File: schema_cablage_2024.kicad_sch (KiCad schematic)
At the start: 64 parts, among them M1 am-3775a, M2 Motor_DC, P1 SB-50, P2 SB-50, SW1 SW_SPDT, SW2 SW_SPDT, U1 VEX_CTRE_Talon_SRX, U11 REV_Spark_MAX, U12 Limelight, U13 REV_Spark_MAX, U14 Kauai_navX2-MXP, U2 Magnetic_Encoder_AM-3749, U4 CTRE_Pneumatics_Control_Module, U6 Banner_Photoelectric_Sensor_Q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, U9 RoboRIO

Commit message: MaJ librairie + schema
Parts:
- gave numbers to parts that had none: 34
- renumbered F7 to F12, F8 to F13, F9 to F14, F3 to F4, F4 to F5, M2 to M6, M1 to M7, U9 to U11, U12 to U13, U14 to U16, U11 to U17, U13 to U18, U1 to U6, U4 to U7, U2 to U8, U6 to U9
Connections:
- net at U8. (PWM): now also U6. (VIN)
- net at U14. (PWM): no longer U12. (VIN)
- new net: U6. (VIN), U8. (PWM) (x2)
- new net: M11. (IN_C), U17. (VIN-)
- new net: U12. (VIN), U14. (PWM) (x3)
- new net: M12. (IN_C), U18. (VIN-)
- new net: M2. (IN_C), U2. (VIN-)
- new net: M1. (IN_C), U1. (VIN-)
- now unconnected: U14. (PWM), U14. (PWM)
- no-connect marks 42 -> 44
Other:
- moved on the sheet: GN1, GN2, GN3

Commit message: Finalisation du symbole PDH, debut du schema 2024
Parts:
- removed F1: 20A, symbol Device:Fuse_Small
- removed F10, F4, F5, F6, F7, F8, F9: 30A, symbol Device:Polyfuse_Small
- removed F12, F13, F2, F3: 40A, symbol Device:Polyfuse
- removed L1, L2, L3: Solenoid, symbol Device:ElectromagneticActor
- removed M10, M3, M4, M5, M7, M8: am-3775a, symbol Motor:Motor_DC
- removed M11, M12: REV_NEO_Brushless_Motor, symbol FRC_Components:REV_NEO_Brushless_Motor
- removed M6: Motor_DC, symbol Motor:Motor_DC
- removed PS1: CTRE_Power_Distribution_Panel, symbol FRC_Components:CTRE_Power_Distribution_Panel
- removed S1: SW_Pressure_NC, symbol FRC_Components:SW_Pressure_NC
- removed SW1, SW2: SW_SPDT, symbol Switch:SW_SPDT
- removed U10, U15, U3, U4, U5: VEX_CTRE_Victor_SPX, symbol FRC_Components:VEX_CTRE_Victor_SPX
- removed U17, U18: REV_Spark_MAX, symbol FRC_Components:REV_Spark_MAX
- removed U6: VEX_CTRE_Talon_SRX, symbol FRC_Components:VEX_CTRE_Talon_SRX
- removed U7: CTRE_Pneumatics_Control_Module, symbol FRC_Components:CTRE_Pneumatics_Control_Module
- removed U8: Magnetic_Encoder_AM-3749, symbol FRC_Components:Magnetic_Encoder_AM-3749
- added D? (x6): NeoPixel_THT, symbol LED:NeoPixel_THT
- added F? (x4): 40A, symbol Device:Polyfuse_Small
- added F? (x3): 30A, symbol Device:Polyfuse_Small
- added M? (x6): REV_NEO_Brushless_Motor, symbol FRC_Components:REV_NEO_Brushless_Motor
- added PS?: REV_Power_Distribution_Hub, symbol FRC_Components:REV_Power_Distribution_Hub
- added U? (x6): REV_Spark_MAX, symbol FRC_Components:REV_Spark_MAX
- F11: value 5A -> 30A
- U13: value Limelight -> Limelight 3
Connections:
- net CANH: now also PS?. (VOUT9), U?. (VIN-), U?. (VIN-), U?. (VIN-), U?. (VIN-), U?. (VIN-), U?. (VIN-); no longer U11. (~{SPI_CS3})
- net CANL: now also PS?. (VOUT9), U?. (VIN-), U?. (VIN-), U?. (VIN-), U?. (VIN-), U?. (VIN-), U?. (VIN-); no longer U11. (~{SPI_CS3})
- net SIG: now also D?.1 (DOUT), D?.1 (DOUT), D?.1 (DOUT), D?.1 (DOUT), D?.4 (DIN), D?.4 (DIN), D?.4 (DIN), D?.4 (DIN), D?.4 (DIN), D?.4 (DIN)
- net V+: now also D?.3 (VDD), D?.3 (VDD), D?.3 (VDD), D?.3 (VDD), D?.3 (VDD), D?.3 (VDD), PS?. (VOUT9), U?. (VIN-), U?. (VIN-), U?. (VIN-), U?. (VIN-), U?. (VIN-), U?. (VIN-); no longer U12. (VIN), U13. (V-)
- net V-: now also D?.2 (GND), D?.2 (GND), D?.2 (GND), D?.2 (GND), D?.2 (GND), D?.2 (GND), PS?. (VOUT9), U?. (VIN-), U?. (VIN-), U?. (VIN-), U?. (VIN-), U?. (VIN-), U?. (VIN-); no longer U13. (V-)
- net ΦA: now also M?. (IN_C), M?. (IN_C), M?. (IN_C), M?. (IN_C), M?. (IN_C), M?. (IN_C), U?. (VIN-), U?. (VIN-), U?. (VIN-), U?. (VIN-), U?. (VIN-), U?. (VIN-)
- net ΦB: now also M?. (IN_C), M?. (IN_C), M?. (IN_C), M?. (IN_C), M?. (IN_C), M?. (IN_C), U?. (VIN-), U?. (VIN-), U?. (VIN-), U?. (VIN-), U?. (VIN-), U?. (VIN-)
- net ΦC: now also M?. (IN_C), M?. (IN_C), M?. (IN_C), M?. (IN_C), M?. (IN_C), M?. (IN_C), U?. (VIN-), U?. (VIN-), U?. (VIN-), U?. (VIN-), U?. (VIN-), U?. (VIN-)
- net at SW4.2 (B): no longer U12. (VIN)
- net at U14. (PWM): now also SW5.1 (A), SW6.1 (A); no longer U12. (VIN)
- net at SW3.2 (B): no longer U12. (VIN)
- net at F11.1: now also PS?. (VOUT9)
- net at F11.2: now also PS?. (VOUT9)
- removed net USB: U11. (~{SPI_CS3}), U16. (μUSB)
- new net: M?. (IN_C), U?. (VIN-) (x6)
- new net: F?.1, PS?. (VOUT9) (x7)
- new net: F?.2, PS?. (VOUT9) (x7)
- new net: M2. (IN_C), U2. (VIN-)
- new net: M1. (IN_C), U1. (VIN-)
- no-connect marks 44 -> 104
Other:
- note added: "Et ainsi de suite pour le reste des bandes de DEL"
- note added: "SPARK MAX SWERVE DIRECTION ARRIERE DROIT"
- note added: "SPARK MAX SWERVE DIRECTION ARRIERE GAUCHE"
- note added: "SPARK MAX SWERVE DIRECTION AVANT DROIT"
- note added: "SPARK MAX SWERVE DIRECTION AVANT GAUCHE"
- note added: "SPARK MAX SWERVE PROPULSION ARRIERE DROIT"
- note added: "SPARK MAX SWERVE PROPULSION ARRIERE GAUCHE"
- note added: "SPARK MAX SWERVE PROPULSION AVANT DROIT"
- note added: "SPARK MAX SWERVE PROPULSION AVANT GAUCHE"
- note removed: "Compresseur"
- note removed: "FWD LIMIT"
- note removed: "Interrupteur à pression — réservoir d'air"
- note removed: "PCM (CAN 0)"
- note removed: "PDP (CAN 0)"
- note removed: "REV LIMIT"
- note removed: "SPARK MAX BASE (DROIT 1)"
- note removed: "TALON SRX ROTATION RAMASSEUR (CAN 6)"
- note removed: "VICTOR SPX RAMASSEUR (DROIT, CAN 7)"
- note removed: "VICTOR SPX RAMASSEUR (GAUCHE, CAN 3)"
- note removed: "VICTOR SPX ÉLÉVATEUR (#2, ESCLAVE, CAN 5)"
- note removed: "VICTOR SPX ÉLÉVATEUR (#3, ESCLAVE, CAN 14)"
- note removed: "VICTOR SPX ÉLÉVATEUR (#4, ESCLAVE, CAN 15)"
- note removed: "VÉRINS BASCULEUR"
- note removed: "VÉRINS RAMASSEUR"
- note removed: "VÉRINS ÉLÉVATEUR"
- moved on the sheet: B1, CB1, DS1, F11, F14, GN1, GN2, GN3, M1, M2, M9, P1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

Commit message: v1.0
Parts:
- removed D? (x6): NeoPixel_THT, symbol LED:NeoPixel_THT
- removed F14: 10A, symbol Device:Fuse_Small
- removed SW3, SW4, SW5, SW6: SW_SPDT, symbol Switch:SW_SPDT
- removed U14: Magnetic_Encoder_AM-3749, symbol FRC_Components:Magnetic_Encoder_AM-3749
- added D? (x4): NeoPixel_THT, symbol LED:NeoPixel_THT
- added F10, F12, F13, F14, F5, F6, F7, F8, F9: 30A, symbol Device:Polyfuse_Small
- added F2: 10A, symbol Device:Polyfuse_Small
- added F3, F4: 5A, symbol Device:Fuse_Small
- added F?: 10A, symbol Device:Fuse_Small
- added M10, M11, M5, M6, M7, M8: REV_NEO_Brushless_Motor, symbol FRC_Components:REV_NEO_Brushless_Motor
- added M3, M4: am-3775a, symbol Motor:Motor_DC
- added U10, U14, U15, U17, U18, U19: REV_Spark_MAX, symbol FRC_Components:REV_Spark_MAX
- added U3: Limelight 2+, symbol FRC_Components:Limelight
- added U4, U6, U8: CTRE_SRX_Mag_Encoder, symbol FRC_Components:CTRE_SRX_Mag_Encoder
- added U5, U7: VEX_CTRE_Talon_SRX, symbol FRC_Components:VEX_CTRE_Talon_SRX
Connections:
- net CANH: now also U10. (VIN-), U14. (VIN-), U15. (VIN-), U17. (VIN-), U18. (VIN-), U19. (VIN-), U5. (VIN), U7. (VIN)
- net CANL: now also U10. (VIN-), U14. (VIN-), U15. (VIN-), U17. (VIN-), U18. (VIN-), U19. (VIN-), U5. (VIN), U7. (VIN)
- net ETH: now also U3. (V-)
- net SIG: now also D?.1 (DOUT), D?.1 (DOUT), D?.4 (DIN), D?.4 (DIN), D?.4 (DIN), D?.4 (DIN)
- net V+: now also U12. (VIN), U13. (V-), D?.3 (VDD), D?.3 (VDD), D?.3 (VDD), D?.3 (VDD), U10. (VIN-), U14. (VIN-), U15. (VIN-), U17. (VIN-), U18. (VIN-), U19. (VIN-), U3. (V-), U5. (VIN), U7. (VIN); no longer M9.1 (+)
- net V-: now also U13. (V-), D?.2 (GND), D?.2 (GND), D?.2 (GND), D?.2 (GND), U10. (VIN-), U14. (VIN-), U15. (VIN-), U17. (VIN-), U18. (VIN-), U19. (VIN-), U3. (V-), U5. (VIN), U7. (VIN); no longer M9.2 (-)
- net ΦA: now also M10. (IN_C), M11. (IN_C), M5. (IN_C), M6. (IN_C), M7. (IN_C), M8. (IN_C), U10. (VIN-), U14. (VIN-), U15. (VIN-), U17. (VIN-), U18. (VIN-), U19. (VIN-)
- net ΦB: now also M10. (IN_C), M11. (IN_C), M5. (IN_C), M6. (IN_C), M7. (IN_C), M8. (IN_C), U10. (VIN-), U14. (VIN-), U15. (VIN-), U17. (VIN-), U18. (VIN-), U19. (VIN-)
- net ΦC: now also M10. (IN_C), M11. (IN_C), M5. (IN_C), M6. (IN_C), M7. (IN_C), M8. (IN_C), U10. (VIN-), U14. (VIN-), U15. (VIN-), U17. (VIN-), U18. (VIN-), U19. (VIN-)
- new net: F4.1, PS?. (VOUT9)
- new net: F4.2, PS?. (VOUT9)
- new net: M11. (IN_C), U19. (VIN-)
- new net: F9.1, PS?. (VOUT9)
- new net: F9.2, PS?. (VOUT9)
- new net: M?. (IN_C), U?. (VIN-) (x6)
- new net: M6. (IN_C), U14. (VIN-)
- new net: M10. (IN_C), U18. (VIN-)
- new net: F14.1, PS?. (VOUT9)
- new net: F14.2, PS?. (VOUT9)
- new net: F10.1, PS?. (VOUT9)
- new net: F10.2, PS?. (VOUT9)
- new net: M7. (IN_C), U15. (VIN-)
- new net: F8.1, PS?. (VOUT9)
- new net: F8.2, PS?. (VOUT9)
- new net: F13.1, PS?. (VOUT9)
- new net: F13.2, PS?. (VOUT9)
- new net: M5. (IN_C), U10. (VIN-)
- new net: F5.1, PS?. (VOUT9)
- new net: F5.2, PS?. (VOUT9)
- new net: M2. (IN_C), U2. (VIN-)
- new net: M1. (IN_C), U1. (VIN-)
- new net: F?.1, PS?. (VOUT9)
- new net: F?.2, PS?. (VOUT9)
- new net: F6.1, PS?. (VOUT9)
- new net: F6.2, PS?. (VOUT9)
- new net: F12.1, PS?. (VOUT9)
- new net: F12.2, PS?. (VOUT9)
- new net: F3.1, PS?. (VOUT9)
- new net: F3.2, PS?. (VOUT9)
- new net: F2.1, PS?. (VOUT9)
- new net: F2.2, PS?. (VOUT9)
- new net: F7.1, PS?. (VOUT9)
- new net: F7.2, PS?. (VOUT9)
- new net: M8. (IN_C), U17. (VIN-)
- new net M+: M3.1 (+), M4.1 (+), M9.1 (+), U12. (VIN), U5. (VIN), U7. (VIN)
- new net M-: M3.2 (-), M4.2 (-), M9.2 (-), U12. (VIN), U5. (VIN), U7. (VIN)
- no-connect marks 104 -> 170
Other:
- note added: "24 DEL/bande. Seulement 2 de représentées."
- note added: "ARRIERE"
- note added: "ATTENTION: Certaines des broches (3, 6) des breakouts ne doivent pas être utilisées."
- note added: "AVANT"
- note added: "Breakout board"
- note added: "Câble gainé pour l'articulation 8 fils seulement au lieu de 10"
- note added: "Les broches de même numéro sont reliées."
- note added: "Nappe de fils plate"
- note added: "SPARK MAX ELEVATEUR DROIT"
- note added: "SPARK MAX ELEVATEUR GAUCHE"
- note added: "SPARK MAX PROPULSION LANCEUR DROIT"
- note added: "SPARK MAX PROPULSION LANCEUR GAUCHE"
- note added: "SPARK MAX RAMASSEUR COURROIE DU BAS"
- note added: "SPARK MAX RAMASSEUR COURROIE DU HAUT"
- note added: "TALON SRX ANGLE LANCEUR"
- note added: "TALON SRX BRAS PRIMAIRE"
- note added: "TALON SRX BRAS SECONDAIRE"
- note removed: "Et ainsi de suite pour le reste des bandes de DEL"
- note removed: "FWD LIMIT 1"
- note removed: "FWD LIMIT 2"
- note removed: "REV LIMIT 1"
- note removed: "REV LIMIT 2"
- note removed: "SPARK MAX BASE (DROIT 2)"
- note removed: "SPARK MAX BASE (GAUCHE 1)"
- note removed: "TALON SRX ÉLÉVATEUR (#1, MAÎTRE, CAN 4)"
- title: Schéma de câblage Swerve 2024 -> Schéma de câblage Disc-O 2024
- moved on the sheet: CB1, DS1, F11, F?, GN1, GN2, GN3, M1, M2, M9, M?, P1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

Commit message: v1.1
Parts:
- removed M1, M2, M? (x6): REV_NEO_Brushless_Motor, symbol FRC_Components:REV_NEO_Brushless_Motor
- removed U1, U2, U? (x6): REV_Spark_MAX, symbol FRC_Components:REV_Spark_MAX
- added U4: Banner_Photoelectric_Sensor_QS18VN6LP, symbol FRC_Components:Banner_Photoelectric_Sensor_QS18VN6LP
- F6: renamed from F2; value 10A -> 20A
- gave numbers to parts that had none: 13
- renumbered F4 to F11, F5 to F14, F6 to F15, F13 to F16, F12 to F17, F7 to F18, F8 to F19, F11 to F2, F14 to F3, F10 to F4, F9 to F5, F3 to F9, GN3 to GN1, GN1 to GN2, GN2 to GN3, M6 to M1, M5 to M2, M4 to M3, M9 to M4, M3 to M5, M7 to M6, M8 to M7, M10 to M8, M11 to M9, U14 to U1, U16 to U10, U8 to U11, U4 to U12, U5 to U13, U15 to U14, U17 to U15, U18 to U16, U19 to U17, U6 to U18, U10 to U2, U9 to U3, U11 to U5, U3 to U6, U13 to U7, U7 to U8, U12 to U9
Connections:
- net CANH: now also U5. (~{SPI_CS3})
- net CANL: now also U5. (~{SPI_CS3})
- net SIG: now also U4. (V-)
- net V+: now also U4. (V-)
- net V-: now also U4. (V-)
- new net: M9. (IN_C), U17. (VIN-)
- new net: M1. (IN_C), U1. (VIN-)
- new net: M8. (IN_C), U16. (VIN-)
- new net: M6. (IN_C), U14. (VIN-)
- new net: M2. (IN_C), U2. (VIN-)
- new net: M7. (IN_C), U15. (VIN-)
- no-connect marks 170 -> 165
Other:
- added sheet Module Swerve arrière droit (module_swerve.kicad_sch)
- added sheet Module Swerve arrière gauche (module_swerve.kicad_sch)
- added sheet Module Swerve avant droit (module_swerve.kicad_sch)
- added sheet Module Swerve avant gauche (module_swerve.kicad_sch)
- note added: "2x Bornier Wago 5 ports"
- note removed: "20 AWG"
- note removed: "SPARK MAX SWERVE DIRECTION ARRIERE DROIT"
- note removed: "SPARK MAX SWERVE DIRECTION ARRIERE GAUCHE"
- note removed: "SPARK MAX SWERVE DIRECTION AVANT DROIT"
- note removed: "SPARK MAX SWERVE DIRECTION AVANT GAUCHE"
- note removed: "SPARK MAX SWERVE PROPULSION ARRIERE DROIT"
- note removed: "SPARK MAX SWERVE PROPULSION ARRIERE GAUCHE"
- note removed: "SPARK MAX SWERVE PROPULSION AVANT DROIT"
- note removed: "SPARK MAX SWERVE PROPULSION AVANT GAUCHE"
- moved on the sheet: B1, CB1, D1, D2, D3, D4, DS1, F1, F10, F11, F12, F13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

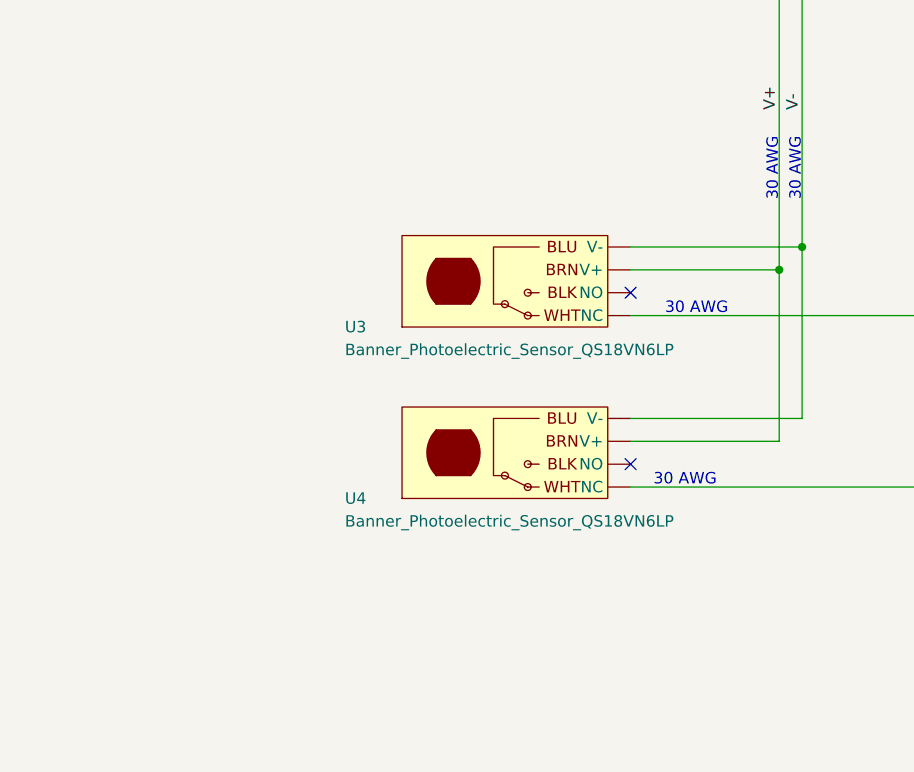
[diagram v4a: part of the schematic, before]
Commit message: v1.2: added photoelectric sensor labels
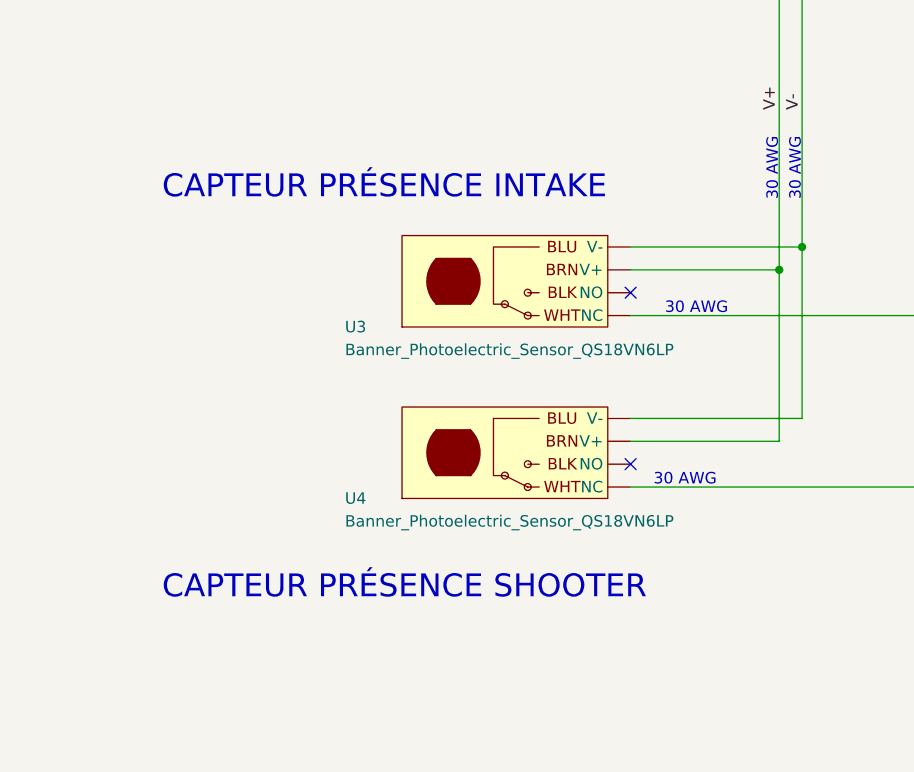
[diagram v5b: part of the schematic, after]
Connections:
- new net: M9. (IN_C), U17. (VIN-)
- new net: M1. (IN_C), U1. (VIN-)
- new net: M8. (IN_C), U16. (VIN-)
- new net: M6. (IN_C), U14. (VIN-)
- new net: M2. (IN_C), U2. (VIN-)
- new net: M7. (IN_C), U15. (VIN-)
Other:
- note added: "CAPTEUR PRÉSENCE INTAKE"
- note added: "CAPTEUR PRÉSENCE SHOOTER"
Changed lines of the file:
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@@
   (title_block
     (title "Schéma de câblage Disc-O 2024")
-    (date "2024-02-04")
-    (rev "1.1")
+    (date "2024-02-06")
+    (rev "1.2")
     (company "ASTRO 7605 (2024)")
   )
@@
     (effects (font (size 1.27 1.27)) (justify left bottom))
   )
+  (text "CAPTEUR PRÉSENCE SHOOTER" (at 201.93 452.12 0)
+    (effects (font (size 2.54 2.54)) (justify left bottom))
+  )
   (text "SPARK MAX\nRAMASSEUR\nCOURROIE DU HAUT" (at 693.42 394.97 0)
     (effects (font (size 2.54 2.54)) (justify left bottom))
@@
     (effects (font (size 1.27 1.27)) (justify left bottom))
   )
+  (text "CAPTEUR PRÉSENCE INTAKE" (at 201.93 407.67 0)
+    (effects (font (size 2.54 2.54)) (justify left bottom))
+  )
   (text "12 AWG" (at 283.21 127 0)

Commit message: v1.3: fixed typo
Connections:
- new net: M9. (IN_C), U17. (VIN-)
- new net: M1. (IN_C), U1. (VIN-)
- new net: M8. (IN_C), U16. (VIN-)
- new net: M6. (IN_C), U14. (VIN-)
- new net: M2. (IN_C), U2. (VIN-)
- new net: M7. (IN_C), U15. (VIN-)
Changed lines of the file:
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@@
     (effects (font (size 1.27 1.27)) (justify left bottom))
   )
-  (text "SPARK MAX\nPROPULSION LANCEUR\nDROIT" (at 137.16 222.25 0)
+  (text "SPARK MAX\nPROPULSION LANCEUR\nGAUCHE" (at 137.16 222.25 0)
     (effects (font (size 2.54 2.54)) (justify left bottom))
   )
@@
     (effects (font (size 1.27 1.27)) (justify left bottom))
   )
-  (text "SPARK MAX\nPROPULSION LANCEUR\nGAUCHE" (at 135.89 137.16 0)
+  (text "SPARK MAX\nPROPULSION LANCEUR\nDROIT" (at 135.89 137.16 0)
     (effects (font (size 2.54 2.54)) (justify left bottom))
   )

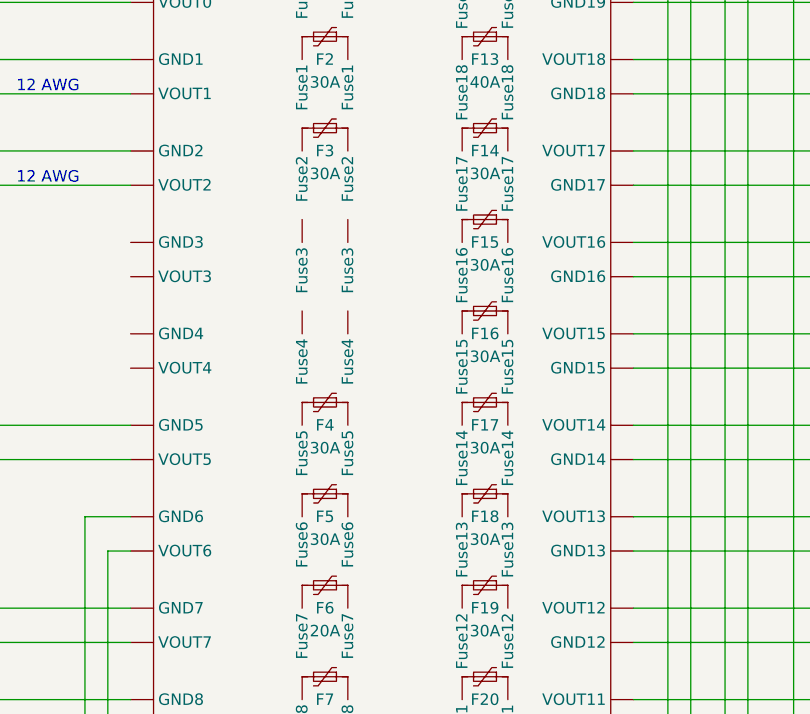
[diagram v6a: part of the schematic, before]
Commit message: Modify some fuses to 40A
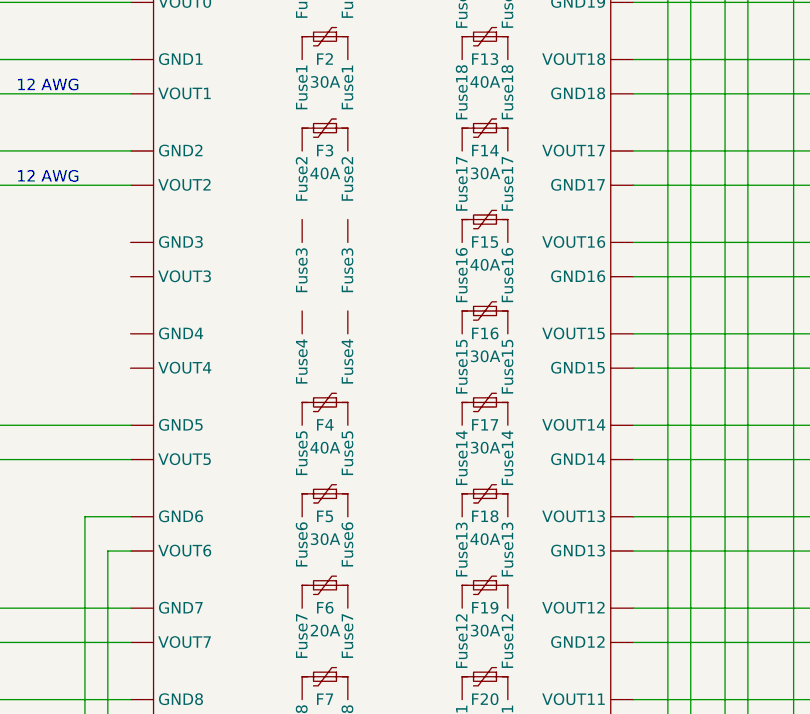
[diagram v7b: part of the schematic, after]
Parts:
- F15, F18, F3, F4: value 30A -> 40A
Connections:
- new net: M9. (IN_C), U17. (VIN-)
- new net: M1. (IN_C), U1. (VIN-)
- new net: M8. (IN_C), U16. (VIN-)
- new net: M6. (IN_C), U14. (VIN-)
- new net: M2. (IN_C), U2. (VIN-)
- new net: M7. (IN_C), U15. (VIN-)
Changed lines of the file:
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@@
   (title_block
     (title "Schéma de câblage Disc-O 2024")
-    (date "2024-02-06")
-    (rev "1.2")
+    (date "2024-02-12")
+    (rev "1.4")
     (company "ASTRO 7605 (2024)")
   )
@@
       (effects (font (size 1.27 1.27)))
     )
-    (property "Value" "30A" (at 317.5 146.05 90)
+    (property "Value" "40A" (at 317.5 146.05 90)
       (effects (font (size 1.27 1.27)))
     )
@@
       (effects (font (size 1.27 1.27)))
     )
-    (property "Value" "30A" (at 317.5 176.53 90)
+    (property "Value" "40A" (at 317.5 176.53 90)
       (effects (font (size 1.27 1.27)))
     )
@@
       (effects (font (size 1.27 1.27)))
     )
-    (property "Value" "30A" (at 335.28 156.21 90)
+    (property "Value" "40A" (at 335.28 156.21 90)
       (effects (font (size 1.27 1.27)))
     )
@@
       (effects (font (size 1.27 1.27)))
     )
-    (property "Value" "30A" (at 335.28 186.69 90)
+    (property "Value" "40A" (at 335.28 186.69 90)
       (effects (font (size 1.27 1.27)))
     )

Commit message: Ajout Orange Pi + sous-systeme vision
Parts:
- removed F11: 5A, symbol Device:Fuse_Small
- removed U6: Limelight 2+, symbol FRC_Components:Limelight
- removed U7: Limelight 3, symbol FRC_Components:Limelight
- added VR2: Mean_Well_RSD-60G-5, symbol FRC_Components:Mean_Well_RSD-60G-5
- F9: value 5A -> 10A
- renumbered U12 to U10, U13 to U11, U14 to U12, U15 to U13, U16 to U14, U17 to U15, U18 to U16, U8 to U6, U9 to U7, U10 to U8, U11 to U9
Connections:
- net V+: now also VR2. (FRAME_GND)
- net V-: now also VR2. (FRAME_GND)
- new net: M9. (IN_C), U15. (VIN-)
- new net: M1. (IN_C), U1. (VIN-)
- new net: M8. (IN_C), U14. (VIN-)
- new net: M6. (IN_C), U12. (VIN-)
- new net: M2. (IN_C), U2. (VIN-)
- new net: M7. (IN_C), U13. (VIN-)
- new net Sous-système vision/GND: VR2. (FRAME_GND)
- new net Sous-système vision/VIN: VR2. (FRAME_GND)
- no-connect marks 165 -> 167
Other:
- added sheet Sous-système vision (sous_systeme_vision.kicad_sch)
